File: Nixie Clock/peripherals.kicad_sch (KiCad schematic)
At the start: 64 parts, among them SW2 RotaryEncoder_Switch, SW7 RotaryEncoder_Switch, SW8 SW_Nidec_CAS-120A1, U10 SI4732-A10-GS, U14 PCM5102, U15 TPA2016D2RTJR, U5 DS3231M, Y2 SG-210STF

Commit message: PCB routed
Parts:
- removed AE3: FM, symbol Device:Antenna
- removed AE4: AM, symbol Device:Antenna
- removed C48: 5pF, symbol Device:C_Polarized
- removed C64, C68, C69: 100nF, symbol Device:C
- removed C65, C67: 10uF, symbol Device:C
- removed D1, D2, D22, D3, D4: WS2812B, LED_SMD:LED_WS2812B_PLCC4_5.0x5.0mm_P3.2mm, symbol LED:WS2812B
- removed D6: D, symbol Device:D
- removed FB3, FB4: FerriteBead, symbol Device:FerriteBead
- removed L1: 500uH, symbol Device:L_Ferrite
- added C13, C15: 1uF, Capacitor_SMD:C_0603_1608Metric, symbol Device:C
- added C16, C20, C21, C24, C25, C26, C27, C29, C33: 100nF, Capacitor_SMD:C_0603_1608Metric, symbol Device:C
- added C22: 5pF, Capacitor_SMD:C_0603_1608Metric, symbol Device:C
- added D13, D14, D15, D16, D17: WS2812B, LED_SMD:LED_WS2812B_PLCC4_5.0x5.0mm_P3.2mm, symbol LED:WS2812B
- added D19: BAT54J, Diode_SMD:D_SOD-323F, symbol Diode:BAT54J
- added J4: FM, Connector_Coaxial:SMA_Amphenol_901-144_Vertical, symbol Connector:Conn_Coaxial
- added J5: AM, Connector_JST:JST_XH_B2B-XH-A_1x02_P2.50mm_Vertical, symbol Connector_Generic:Conn_01x02
- added U5: 74AHCT1G125, Package_TO_SOT_SMD:SOT-23-5, symbol 74xGxx:74AHCT1G125
- BT1: footprint (none) -> Battery:BatteryHolder_Keystone_1060_1x2032
- C12: renamed from C61; footprint (none) -> Capacitor_SMD:C_0603_1608Metric
- C14: renamed from C62; footprint (none) -> Capacitor_SMD:C_0603_1608Metric
- C17: renamed from C47; footprint (none) -> Capacitor_SMD:C_0603_1608Metric
- C18: renamed from C63; footprint (none) -> Capacitor_SMD:C_0603_1608Metric
- C19: renamed from C49; footprint (none) -> Capacitor_SMD:C_0603_1608Metric
- C23: renamed from C66; footprint (none) -> Capacitor_SMD:C_0603_1608Metric
- C28: renamed from C50; footprint (none) -> Capacitor_SMD:C_0603_1608Metric
- C30: renamed from C52; footprint (none) -> Capacitor_SMD:C_0603_1608Metric
- C31: renamed from C53; footprint (none) -> Capacitor_SMD:C_0603_1608Metric
- C32: renamed from C51; footprint (none) -> Capacitor_SMD:C_0603_1608Metric
- C34: renamed from C54; footprint (none) -> Capacitor_SMD:C_0603_1608Metric
- C35: renamed from C55; footprint (none) -> Capacitor_SMD:C_0603_1608Metric
- C36: renamed from C56; footprint (none) -> Capacitor_SMD:C_0603_1608Metric
- C37: renamed from C57; footprint (none) -> Capacitor_SMD:C_0603_1608Metric
- C38: renamed from C58; footprint (none) -> Capacitor_SMD:C_0603_1608Metric
- C39: renamed from C60; footprint (none) -> Capacitor_SMD:C_0603_1608Metric
- C40: renamed from C59; footprint (none) -> Capacitor_SMD:C_0603_1608Metric
- C41: renamed from C21; footprint (none) -> Capacitor_SMD:C_0603_1608Metric
- D18: renamed from D23; footprint (none) -> LED_SMD:LED_0201_0603Metric
- LS1: renamed from LS3; footprint (none) -> Connector_JST:JST_XH_B2B-XH-A_1x02_P2.50mm_Vertical
- LS2: renamed from LS4; footprint (none) -> Connector_JST:JST_XH_B2B-XH-A_1x02_P2.50mm_Vertical
- R18: renamed from R76; footprint (none) -> Resistor_SMD:R_0603_1608Metric
- R19: renamed from R77; footprint (none) -> Resistor_SMD:R_0603_1608Metric
- R20: renamed from R81; footprint (none) -> Resistor_SMD:R_0603_1608Metric
- R21: renamed from R52; footprint (none) -> Resistor_SMD:R_0603_1608Metric
- R22: renamed from R78; footprint (none) -> Resistor_SMD:R_0603_1608Metric
- R23: renamed from R79; footprint (none) -> Resistor_SMD:R_0603_1608Metric
- R24: renamed from R80; footprint (none) -> Resistor_SMD:R_0603_1608Metric
- R25: renamed from R55; footprint (none) -> Resistor_SMD:R_0603_1608Metric
- R26: renamed from R70; footprint (none) -> Resistor_SMD:R_0603_1608Metric
- R27: renamed from R71; footprint (none) -> Resistor_SMD:R_0603_1608Metric
- R28: renamed from R54; footprint (none) -> Resistor_SMD:R_0603_1608Metric
- R29: renamed from R53; footprint (none) -> Resistor_SMD:R_0603_1608Metric
- R30: renamed from R72; footprint (none) -> Resistor_SMD:R_0603_1608Metric
- R31: renamed from R73; footprint (none) -> Resistor_SMD:R_0603_1608Metric
- R32: renamed from R74; footprint (none) -> Resistor_SMD:R_0603_1608Metric
- R33: renamed from R75; footprint (none) -> Resistor_SMD:R_0603_1608Metric
- SW4: renamed from SW2; footprint (none) -> Rotary_Encoder:RotaryEncoder_Alps_EC11E-Switch_Vertical_H20mm
- SW5: renamed from SW7; footprint (none) -> Rotary_Encoder:RotaryEncoder_Alps_EC11E-Switch_Vertical_H20mm
- U6: renamed from U10; footprint SOIC_A10-GS_SIL -> SI4732:SOIC_A10-GS_SIL
- Y1: renamed from Y2; value SG-210STF -> OK252032.768KJBA4SL
- renumbered D5 to D12, SW8 to SW3, U15 to U7, U14 to U8, U5 to U9
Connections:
- net +5VA is gone; now on net +5V: U7.13 (AVDD)
- net GNDA is gone; now on net GND: C14.1, C18.1, U7.3 (AGND)
- net +3.3V: now also U8.17 (XSMT)
- net +5V: now also C13.2, C15.2, C16.2, C20.2, C21.2, C24.1, C25.1, C26.1, C27.1, C29.1, C33.1, D13.1 (VDD), D14.1 (VDD), D15.1 (VDD), D16.1 (VDD), D17.1 (VDD), U5.5 (VCC)
- net GND: now also C13.1, C15.1, C16.1, C20.1, C21.1, C22.1, C24.2, C25.2, C26.2, C27.2, C29.2, C33.2, D13.3 (VSS), D14.3 (VSS), D15.3 (VSS), D16.3 (VSS), D17.3 (VSS), J4.2 (Ext), U5.1, U5.3 (GND); no longer U6.7 (RFGND), U8.17 (XSMT)
- net LEDIN: now also U5.2; no longer R21.1
- net at R19.2, U6.1 (LOUT/DFS): now also C22.2
- net at BT1.1 (+), U9.14 (VBAT): now also D19.1 (K)
- net at R29.1: now also D19.2 (A)
- net at C17.2: now also J4.1 (In)
- net at D12.2 (DOUT): now also D13.4 (DIN)
- net at U7.10 (OUTR+): now also LS2.2; no longer LS2.1
- net at U7.9 (OUTR-): now also LS2.1; no longer LS2.2
- net at C19.2: now also J5.1 (Pin_1)
- new net: D16.2 (DOUT), D17.4 (DIN)
- new net: D15.2 (DOUT), D16.4 (DIN)
- new net: D14.2 (DOUT), D15.4 (DIN)
- new net: D13.2 (DOUT), D14.4 (DIN)
- new net: R21.1, U5.4
- new net: J5.2 (Pin_2), U6.7 (RFGND)
- no-connect marks 4 -> 5
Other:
- title: (none) -> Nixie Clock
- moved on the sheet: C17, C19, C28, C32, D12, R18, R19, R20, R21, R22, SW3, U6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

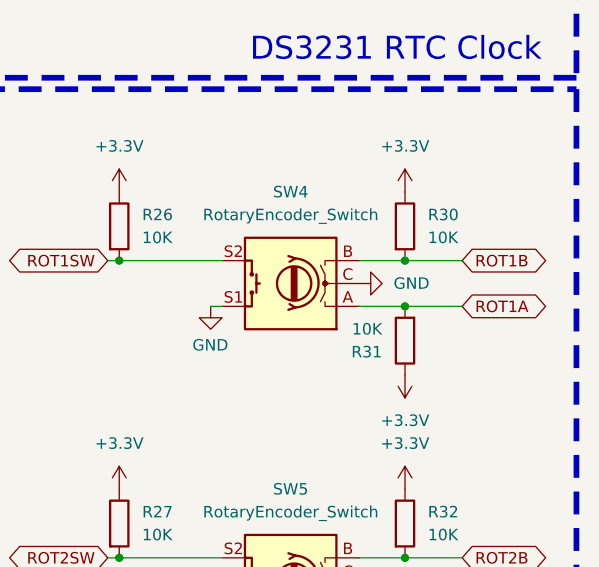
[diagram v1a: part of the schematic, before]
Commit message: Rev2.1 depopulated R30 and R31 pullup resistors
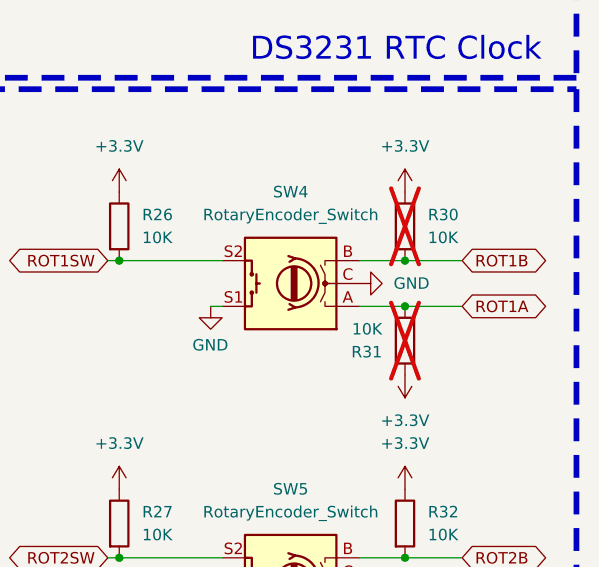
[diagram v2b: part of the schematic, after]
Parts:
- R30, R31: now not fitted
